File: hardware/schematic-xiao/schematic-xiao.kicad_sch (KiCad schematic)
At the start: 20 parts, among them J1 Conn_02x04_Odd_Even, J2 Conn_01x02, SW1 RotaryEncoder, SW2 SW_Push, SW3 SW_Push, SW4 SW_Push, SW5 SW_Push, U1 XIAO ESP32C3, U3 MCP23S17_SP, U4 74HC244

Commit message: Added todo note
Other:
- note added: "See this link."
- note added: "TODO Merge SPI signals into a bus."
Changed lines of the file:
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@@
+	)
+	(rectangle
+		(start 37.465 95.885)
+		(end 77.47 107.315)
+		(stroke
+			(width 0)
+			(type default)
+		)
+		(fill
+			(type none)
+		)
 	)
 	(rectangle
@@
 		)
 	)
+	(text "See this link."
+		(exclude_from_sim no)
+		(at 47.244 102.616 0)
+		(effects
+			(font
+				(size 1.27 1.27)
+			)
+			(href "https://forum.kicad.info/t/how-to-collapse-long-bus-name-with-bus-aliases/35682")
+		)
+	)
+	(text "TODO Merge SPI signals into a bus.\n"
+		(exclude_from_sim no)
+		(at 57.912 99.822 0)
+		(effects
+			(font
+				(size 1.27 1.27)
+				(thickness 0.254)
+				(bold yes)
+			)
+		)
+	)

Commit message: Added SPI bus, UART communication and seperate display processor
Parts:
- added D3: SB140, symbol Device:D_Schottky_Small
- added U5: XIAO ESP32C3, XIAO_ESP32C3:xiao_esp32c3, symbol xiao_esp32c3:XIAO ESP32C3
- J1: Name (none) -> Display Connector
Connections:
- net +5V: now also D3.2 (A)
- net DISP_CS: no longer U1.10 (MISO/IO9/D9)
- net GND: now also U5.13 (GND)
- net MISO-DSIDE: no longer J1.6 (Pin_6)
- net MOSI-DSIDE: no longer J1.7 (Pin_7)
- net MAIN-TX: now reaches U1.7 (D6/IO21/TX)
- net MAIN-TX: now also U5.8 (RX/IO20/D7)
- net MAIN-RX: now reaches U1.8 (RX/IO20/D7)
- net MAIN-RX: now also U5.7 (D6/IO21/TX)
- net DREQ-GPIO8 renamed DREQ
- net GPIO10-XDCS renamed XDCS
- net I04-XCS renamed XCS
- net IO5-SCK renamed RADIO-SCK
- net IO6-MOSI renamed RADIO-MOSI
- net IO7-MISO renamed RADIO-MISO
- net SCK-DSIDE renamed DISPLAY-SCK
- net DISPLAY-SCK: no longer U4.16 (1Y1)
- new net: D3.1 (K), U5.14 (5V/VUSB)
- new net DISP-CS: U5.1 (D0/IO2/A0)
- new net DISP-MISO: J1.6 (Pin_6), U5.10 (MISO/IO9/D9)
- new net DISP-MOSI: J1.7 (Pin_7), U5.11 (MOSI/IO10/D10)
- new net DISP-SCK: U5.9 (SCK/IO8/D8)
- new net RADIO-SCK-DSIDE: U4.16 (1Y1)
- no-connect marks 19 -> 27
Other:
- moved on the sheet: AE1, D2, J1, J2, R1, R2, R3, R4, R5, R6, SW1, SW2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

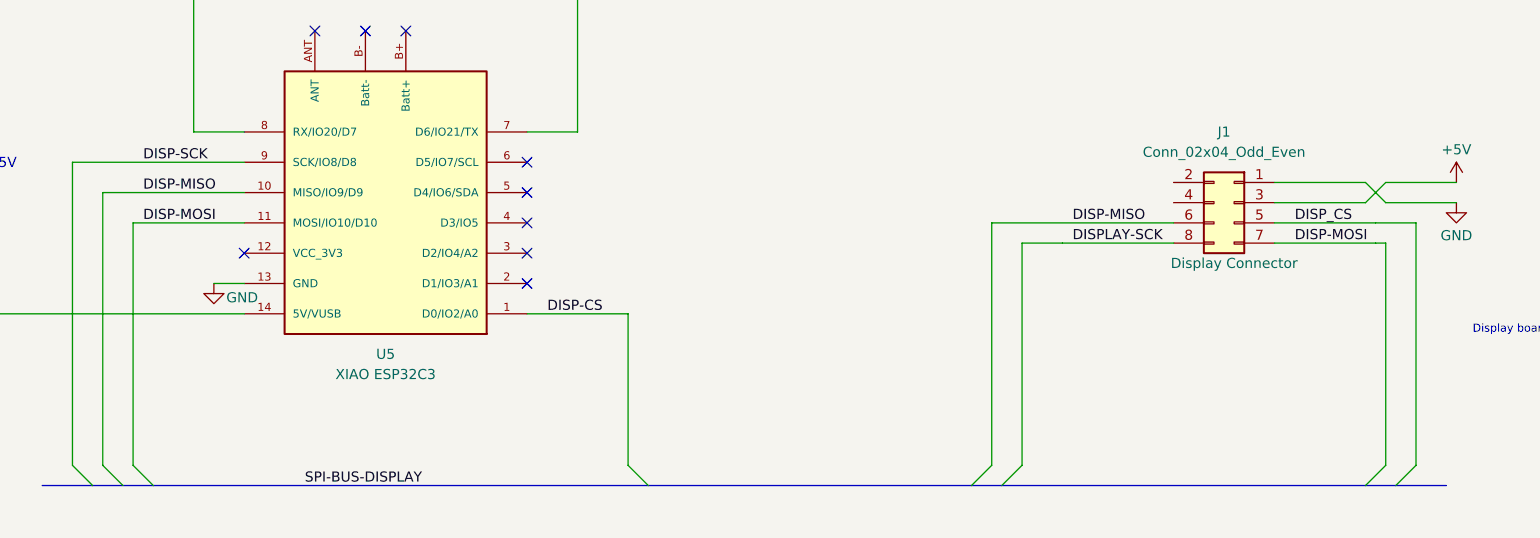
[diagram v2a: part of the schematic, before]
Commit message: Changed signal names from display to ui
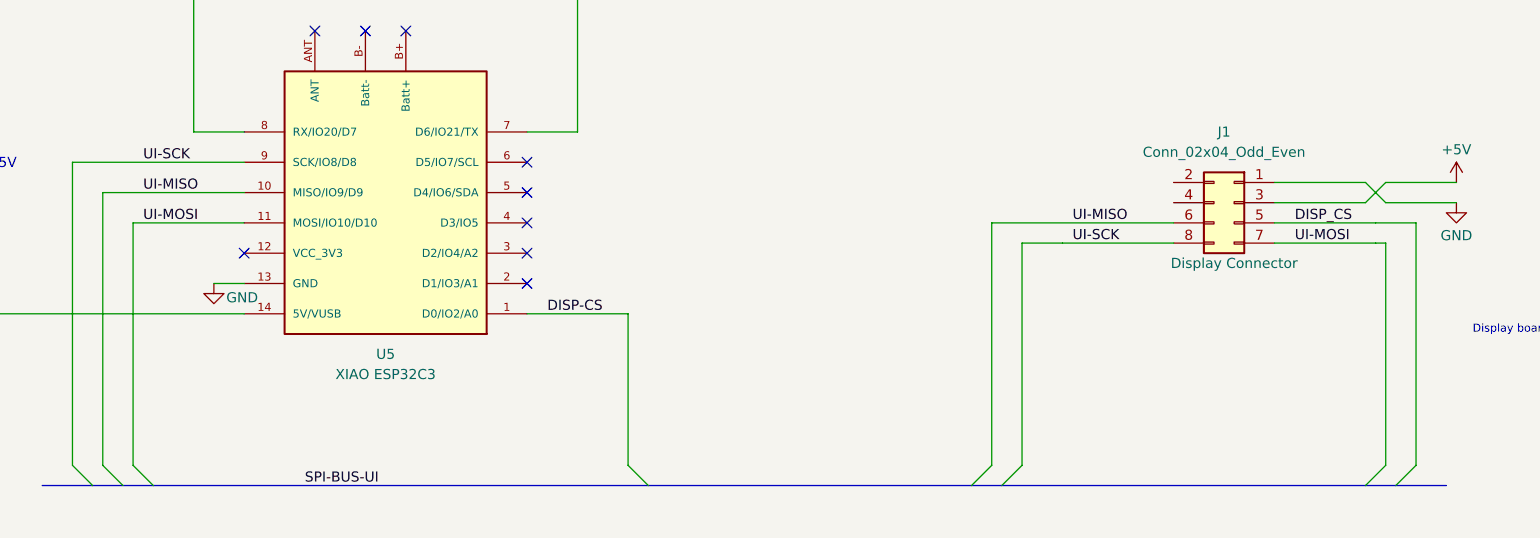
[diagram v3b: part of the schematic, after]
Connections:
- net DISPLAY-SCK is gone; now on net UI-SCK: J1.8 (Pin_8)
- net DISP-MISO renamed UI-MISO
- net DISP-MOSI renamed UI-MOSI
- net DISP-SCK renamed UI-SCK
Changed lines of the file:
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@@
 		)
 	)
-	(label "SPI-BUS-DISPLAY"
+	(label "SPI-BUS-UI"
 		(at 121.92 238.76 0)
 		(effects
@@
 		)
 	)
-	(label "DISP-MOSI"
+	(label "UI-MOSI"
 		(at 246.38 208.28 0)
 		(effects
@@
 		)
 	)
-	(label "DISP-MOSI"
+	(label "UI-MOSI"
 		(at 101.6 205.74 0)
 		(effects
@@
 		)
 	)
-	(label "DISPLAY-SCK"
+	(label "UI-SCK"
 		(at 218.44 208.28 0)
 		(effects
@@
 		)
 	)
-	(label "DISP-MISO"
+	(label "UI-MISO"
 		(at 101.6 201.93 0)
 		(effects
@@
 		)
 	)
-	(label "DISP-SCK"
+	(label "UI-SCK"
 		(at 101.6 198.12 0)
 		(effects
@@
 		)
 	)
-	(label "DISP-MISO"
+	(label "UI-MISO"
 		(at 218.44 205.74 0)
 		(effects

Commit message: Rewired for 2 processors - one for radio, the other for UI
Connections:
- net RADIO-MISO: no longer U3.14 (SO), U4.14 (1Y2)
- net RADIO-MOSI: no longer U3.13 (SI), U4.2 (1A0)
- net RADIO-SCK: no longer U3.12 (SCK), U4.4 (1A1)
- net UI-MISO: now also U3.14 (SO), U4.14 (1Y2); no longer J1.6 (Pin_6)
- net UI-MOSI: now also U3.13 (SI), U4.2 (1A0); no longer J1.7 (Pin_7)
- net UI-SCK: now also U3.12 (SCK), U4.4 (1A1); no longer J1.8 (Pin_8)
- net MUX-CS: now reaches U5.2 (D1/IO3/A1)
- net MISO-DSIDE renamed DISP-MISO
- net DISP-MISO: now also J1.6 (Pin_6)
- net MOSI-DSIDE renamed DISP-MOSI
- net DISP-MOSI: now also J1.7 (Pin_7)
- net RADIO-SCK-DSIDE renamed DISP-SCK
- net DISP-SCK: now also J1.8 (Pin_8)
- no-connect marks 27 -> 28
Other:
- note added: "DISP-MISO is an input and thus the buffer is wired differently."
- note added: "RADIO"
- note added: "USER INTERFACE"
- note removed: "See this link."
- note removed: "TODO Merge SPI signals into a bus."
- moved on the sheet: AE1, D1, D2, D3, J1, J2, R1, R2, R3, R4, R5, R6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
